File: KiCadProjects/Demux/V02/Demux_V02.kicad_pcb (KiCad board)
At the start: 2 copper layers, 90 x 100 mm, 44 parts, among them J1 alimentacao analogica, J10 +3.3Vmux, J11 -9Vmux, J12 -5Vmux, J13 GNDmux, J14 conectorEletrodos, J15 conectorEletrodos, J2 sinais analogicos, J3 comunicacao / sinais digitais, J4 Conn_01x03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

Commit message: correcao sinais de selecao e add capacitores alimentacao
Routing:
- net Earth: vias 1 -> 13
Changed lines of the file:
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@@
 		(tags "C Disc series Radial pin pitch 2.50mm diameter 3.0mm width 1.6mm Capacitor")
 		(property "Reference" "C2-B4"
-			(at 1.25 -2.049999 90)
+			(at 6.66 0.84 270)
 			(layer "F.SilkS")
 			(effects
@@
 		(tags "Resistor Axial_DIN0207 series Axial Horizontal pin pitch 7.62mm 0.25W = 1/4W length 6.3mm diameter 2.5mm")
 		(property "Reference" "R4"
-			(at -1.952 -0.58 90)
+			(at -0.24 2 180)
 			(layer "F.SilkS")
 			(effects
@@
 		(tags "C Disc series Radial pin pitch 2.50mm diameter 3.0mm width 1.6mm Capacitor")
 		(property "Reference" "C2-B3"
-			(at 1.25 -2.05 0)
+			(at 1.43 2.18 0)
 			(layer "F.SilkS")
 			(effects
@@
 		(tags "Resistor Axial_DIN0207 series Axial Horizontal pin pitch 7.62mm 0.25W = 1/4W length 6.3mm diameter 2.5mm")
 		(property "Reference" "R3"
-			(at -1.952 -0.274 90)
+			(at -0.34 -2.1 180)
 			(layer "F.SilkS")
 			(effects
@@
 		(tags "CP Radial series Radial pin pitch 2.50mm diameter 5mm height 7mm Electrolytic Capacitor")
 		(property "Reference" "C1-5A1"
-			(at 1.25 -3.75 90)
+			(at -3.6049 2.48 90)
 			(layer "F.SilkS")
 			(effects
@@
 		(tags "C Disc series Radial pin pitch 2.50mm diameter 3.0mm width 1.6mm Capacitor")
 		(property "Reference" "C1-A4"
-			(at 1.25 -2.049999 90)
+			(at 6.54 0.13 90)
 			(layer "F.SilkS")
 			(effects
@@
 		(tags "C Disc series Radial pin pitch 2.50mm diameter 3.0mm width 1.6mm Capacitor")
 		(property "Reference" "C1-A1"
-			(at 1.25 -2.049999 90)
+			(at 7.12 0.1 90)
 			(layer "F.SilkS")
 			(effects
@@
 		(tags "C Disc series Radial pin pitch 2.50mm diameter 3.0mm width 1.6mm Capacitor")
 		(property "Reference" "C1-A3"
-			(at 1.25 -2.049999 90)
+			(at 4.41 -0.02 180)
 			(layer "F.SilkS")
 			(effects
@@
 	)
 	(via
+		(at 164 106)
+		(size 1.2)
+		(drill 0.6)
+		(layers "F.Cu" "B.Cu")
+		(free yes)
+		(net 10)
+	)
+	(via
+		(at 153 103)
+		(size 1.2)
+		(drill 0.6)
+		(layers "F.Cu" "B.Cu")
+		(free yes)
+		(net 10)
+	)
+	(via
+		(at 127.5 60.8)
+		(size 1.2)
+		(drill 0.6)
+		(layers "F.Cu" "B.Cu")
+		(free yes)
+		(net 10)
+	)
+	(via
+		(at 150.9 66.1)
+		(size 1.2)
+		(drill 0.6)
+		(layers "F.Cu" "B.Cu")
+		(free yes)
+		(net 10)
+	)
+	(via
+		(at 115.7 82.2)
+		(size 1.2)
+		(drill 0.6)
+		(layers "F.Cu" "B.Cu")
+		(free yes)
+		(net 10)
+	)
+	(via
+		(at 160.6 101.7)
+		(size 1.2)
+		(drill 0.6)
+		(layers "F.Cu" "B.Cu")
+		(free yes)
+		(net 10)
+	)
+	(via
+		(at 138.7 104.3)
+		(size 1.2)
+		(drill 0.6)
+		(layers "F.Cu" "B.Cu")
+		(free yes)
+		(net 10)
+	)
+	(via
+		(at 155 99)
+		(size 1.2)
+		(drill 0.6)
+		(layers "F.Cu" "B.Cu")
+		(free yes)
+		(net 10)
+	)
+	(via
+		(at 132.1 98.4)
+		(size 1.2)
+		(drill 0.6)
+		(layers "F.Cu" "B.Cu")
+		(free yes)
+		(net 10)
+	)
+	(via
+		(at 147.4 124.4)
+		(size 1.2)
+		(drill 0.6)
+		(layers "F.Cu" "B.Cu")
+		(free yes)
+		(net 10)
+	)
+	(via
+		(at 168.2 102)
+		(size 1.2)
+		(drill 0.6)
+		(layers "F.Cu" "B.Cu")
+		(free yes)
+		(net 10)
+	)
+	(via
 		(at 150.4366 59.4573)
 		(size 1.2)
@@
 		(net 10)
 	)
+	(via
+		(at 123.2 101.3)
+		(size 1.2)
+		(drill 0.6)
+		(layers "F.Cu" "B.Cu")
+		(free yes)
+		(net 10)
+	)

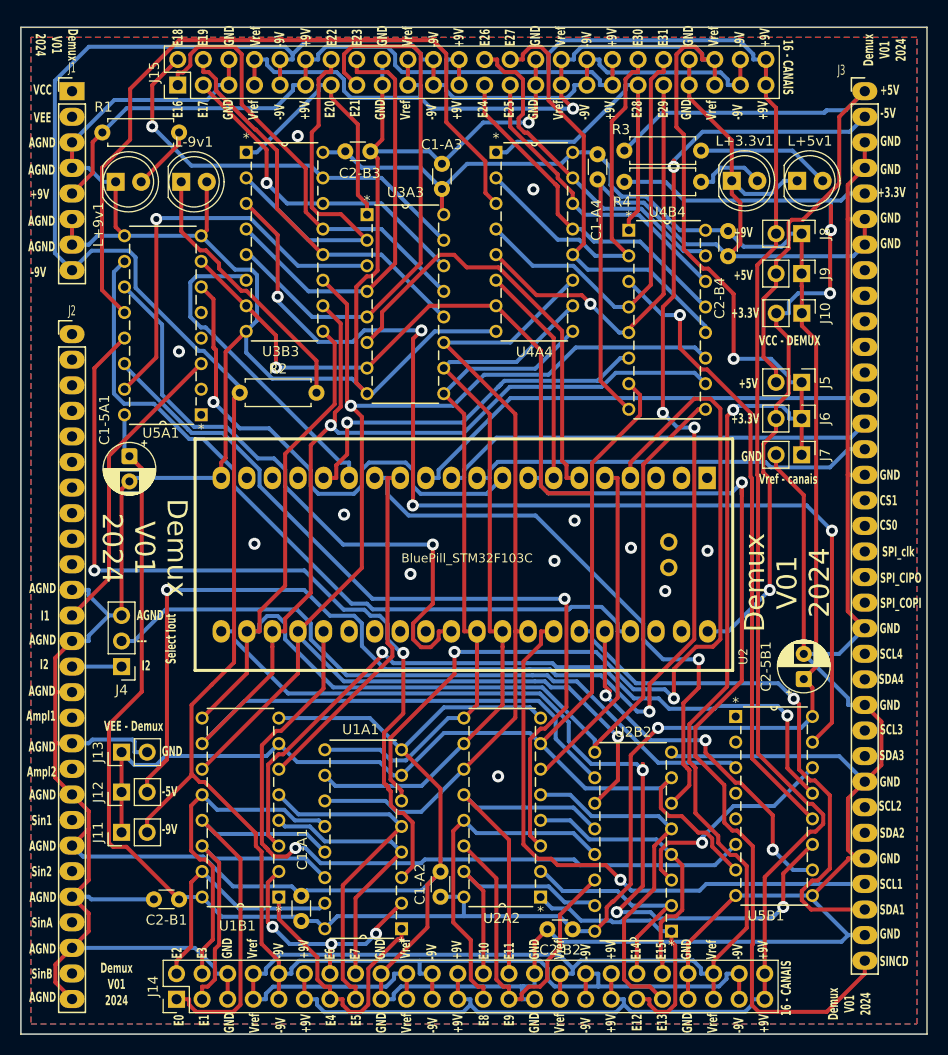
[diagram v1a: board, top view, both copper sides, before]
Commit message: correcao sinais de selecao e add capacitores alimentacao
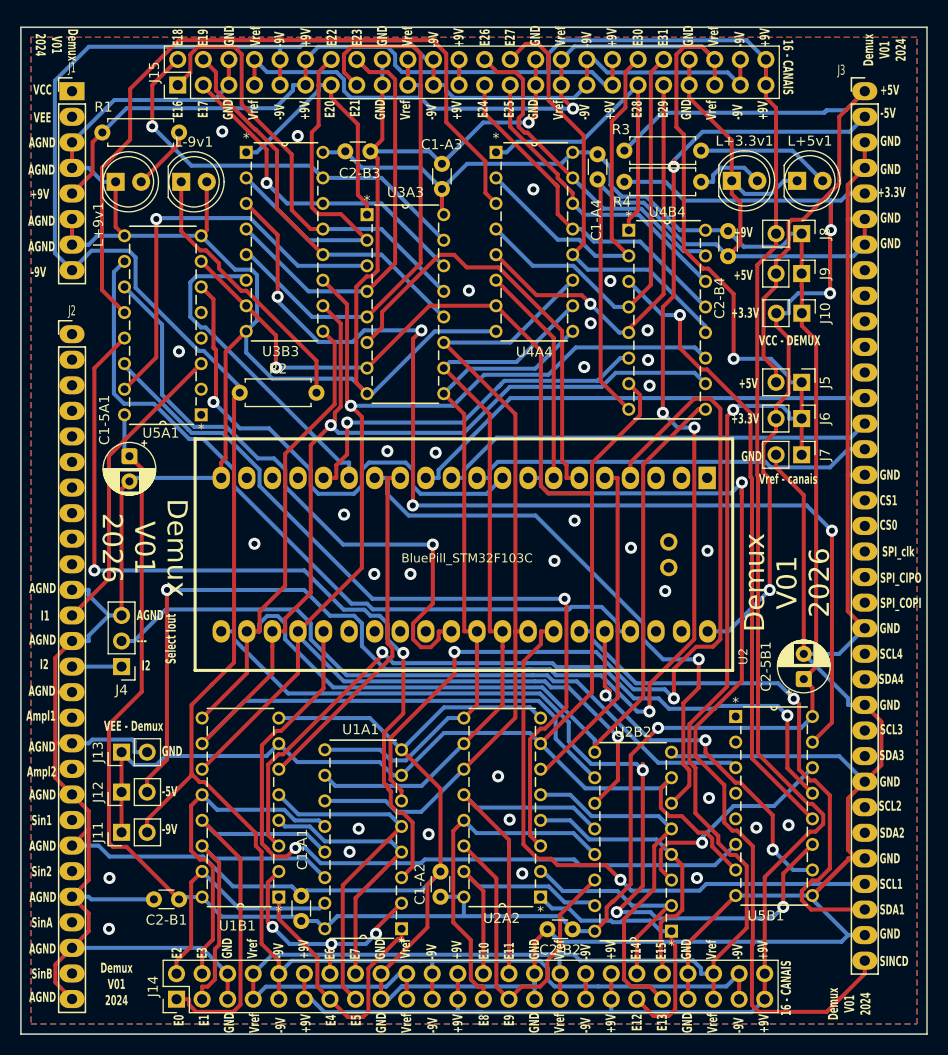
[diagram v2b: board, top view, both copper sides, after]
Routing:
- net Earth: track 694.2 -> 700.2 mm, vias 13 -> 35
- net -9V: track 267.2 -> 261.7 mm
- net +9V: track 258.8 -> 254.7 mm
- net Vref: track 267.6 -> 266.6 mm
- net E23: track 42.1 -> 41.4 mm
- net E9: track 34.2 -> 33.5 mm
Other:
- board text added: "Demux V01 2026"
